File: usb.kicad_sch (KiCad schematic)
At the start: 18 parts, among them J13 USB-C_TYPE-C_16PLT-H6.5, J7 USB-A_USB-303WSD-BRY, U1 AP22615AWU-7

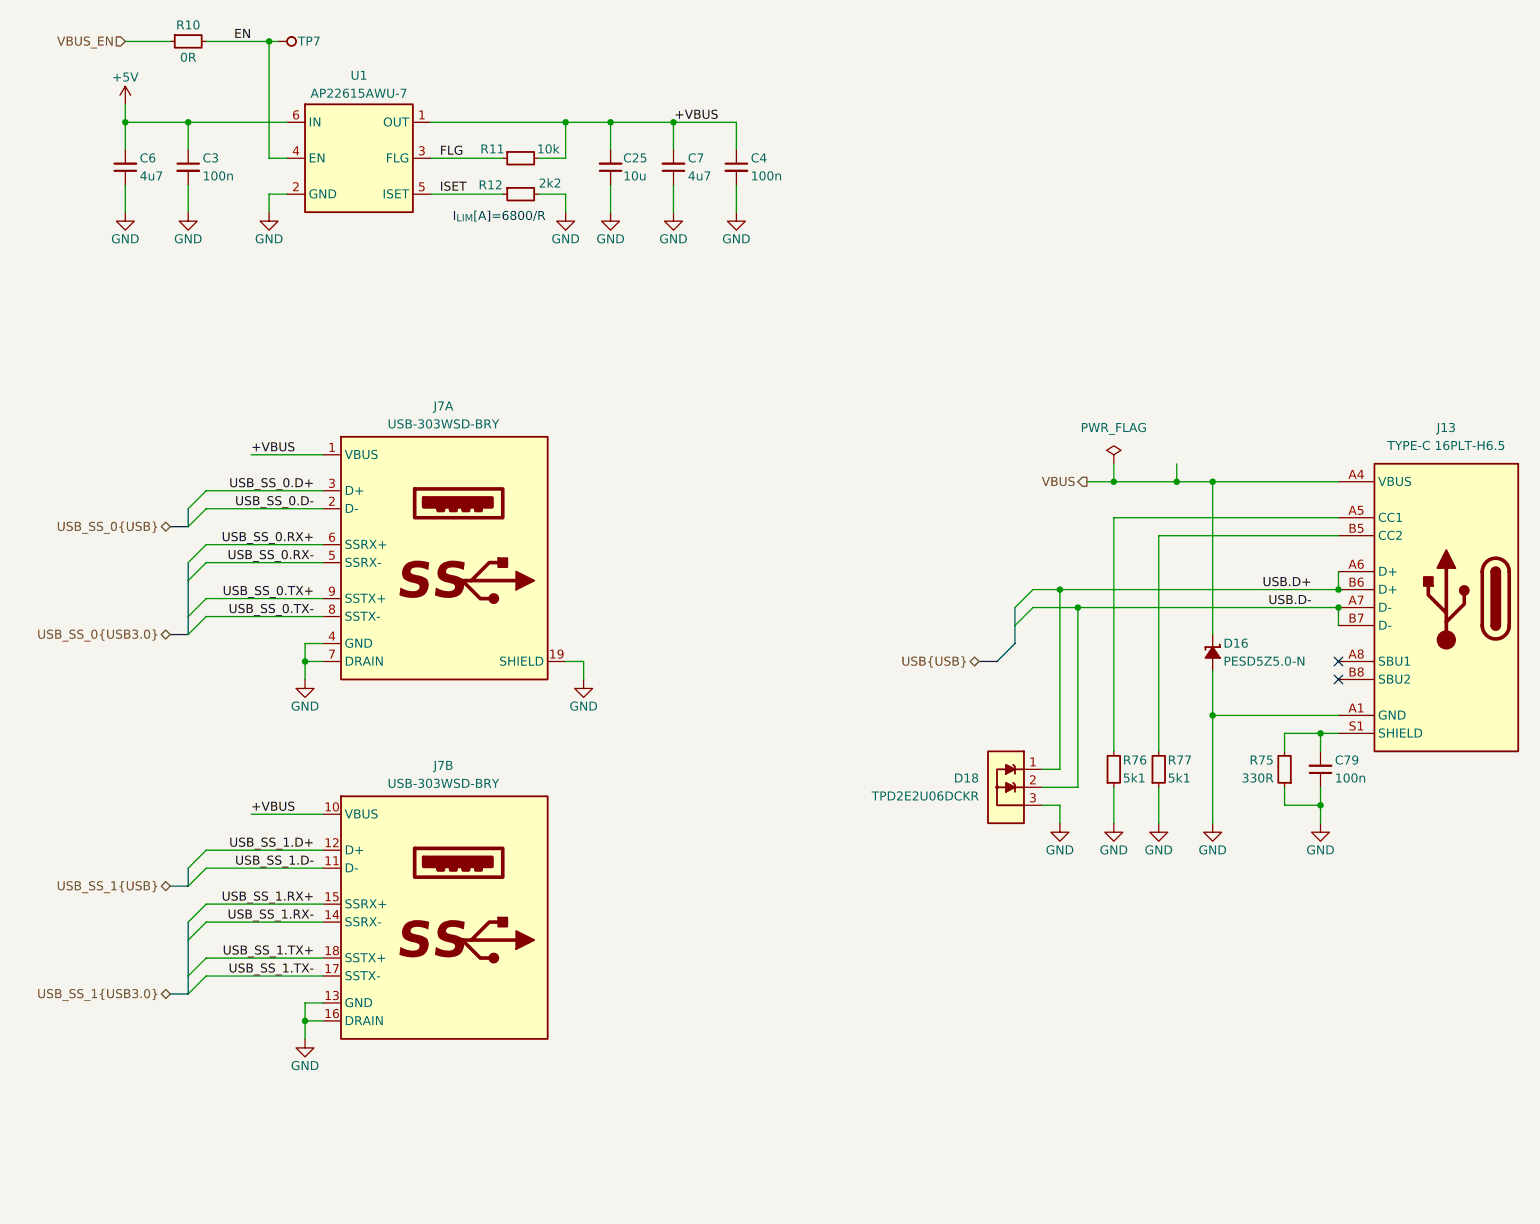
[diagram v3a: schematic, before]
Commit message: [#3] Layout HDMI, PCIe and ETH differential pairs
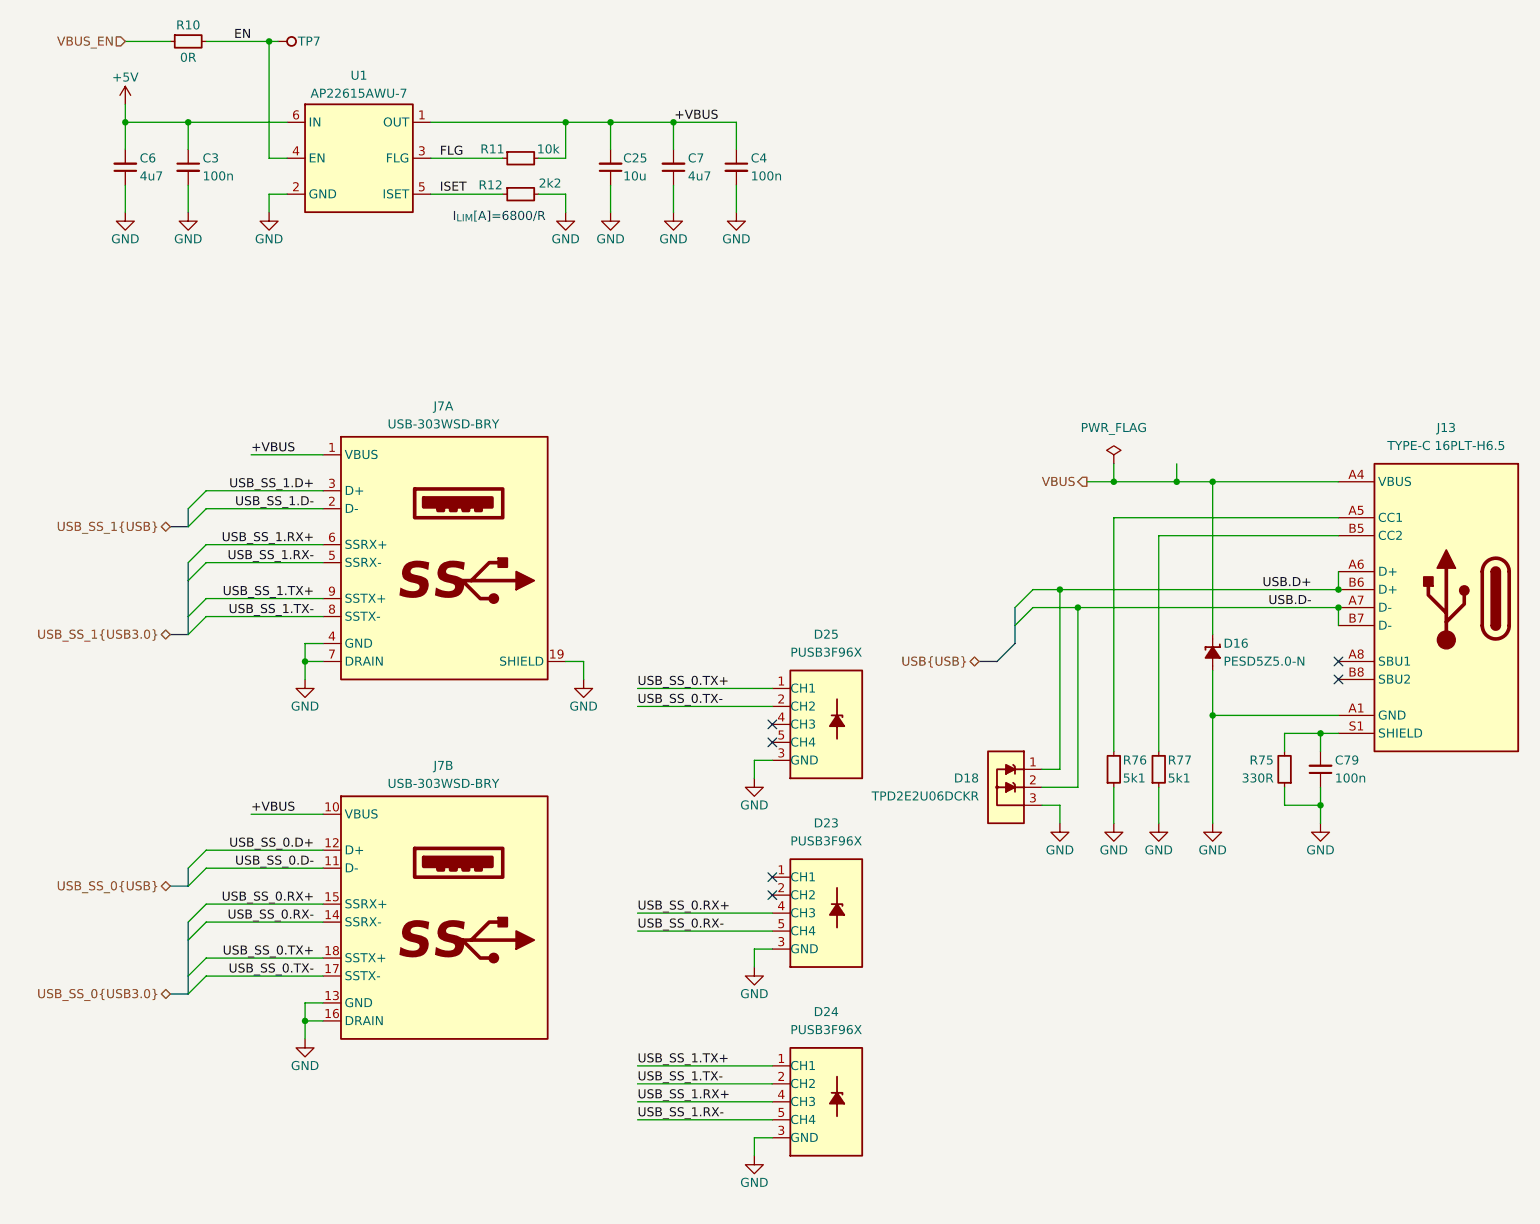
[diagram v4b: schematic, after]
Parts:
- added D23, D24, D25: PUSB3F96X, DW-footprints:SOT1176-1, symbol DW-TVS:PUSB3F96X
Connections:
- net GND: now also D23.3 (GND), D23.8 (GND), D24.3 (GND), D24.8 (GND), D25.3 (GND), D25.8 (GND)
- net USB_SS_0.D+: now also J7.12 (D+); no longer J7.3 (D+)
- net USB_SS_0.D-: now also J7.11 (D-); no longer J7.2 (D-)
- net USB_SS_0.RX+: now also J7.15 (SSRX+), D23.4 (CH3), D23.7 (CH3); no longer J7.6 (SSRX+)
- net USB_SS_0.RX-: now also J7.14 (SSRX-), D23.5 (CH4), D23.6 (CH4); no longer J7.5 (SSRX-)
- net USB_SS_0.TX+: now also J7.18 (SSTX+), D25.1 (CH1), D25.10 (CH1); no longer J7.9 (SSTX+)
- net USB_SS_0.TX-: now also J7.17 (SSTX-), D25.2 (CH2), D25.9 (CH2); no longer J7.8 (SSTX-)
- net USB_SS_1.D+: now also J7.3 (D+); no longer J7.12 (D+)
- net USB_SS_1.D-: now also J7.2 (D-); no longer J7.11 (D-)
- net USB_SS_1.RX+: now also J7.6 (SSRX+), D24.4 (CH3), D24.7 (CH3); no longer J7.15 (SSRX+)
- net USB_SS_1.RX-: now also J7.5 (SSRX-), D24.5 (CH4), D24.6 (CH4); no longer J7.14 (SSRX-)
- net USB_SS_1.TX+: now also J7.9 (SSTX+), D24.1 (CH1), D24.10 (CH1); no longer J7.18 (SSTX+)
- net USB_SS_1.TX-: now also J7.8 (SSTX-), D24.2 (CH2), D24.9 (CH2); no longer J7.17 (SSTX-)
- new net: D25.4 (CH3), D25.7 (CH3)
- new net: D25.5 (CH4), D25.6 (CH4)
- new net: D23.1 (CH1), D23.10 (CH1)
- new net: D23.2 (CH2), D23.9 (CH2)
- no-connect marks 2 -> 6

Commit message: [#3] Layout USB power
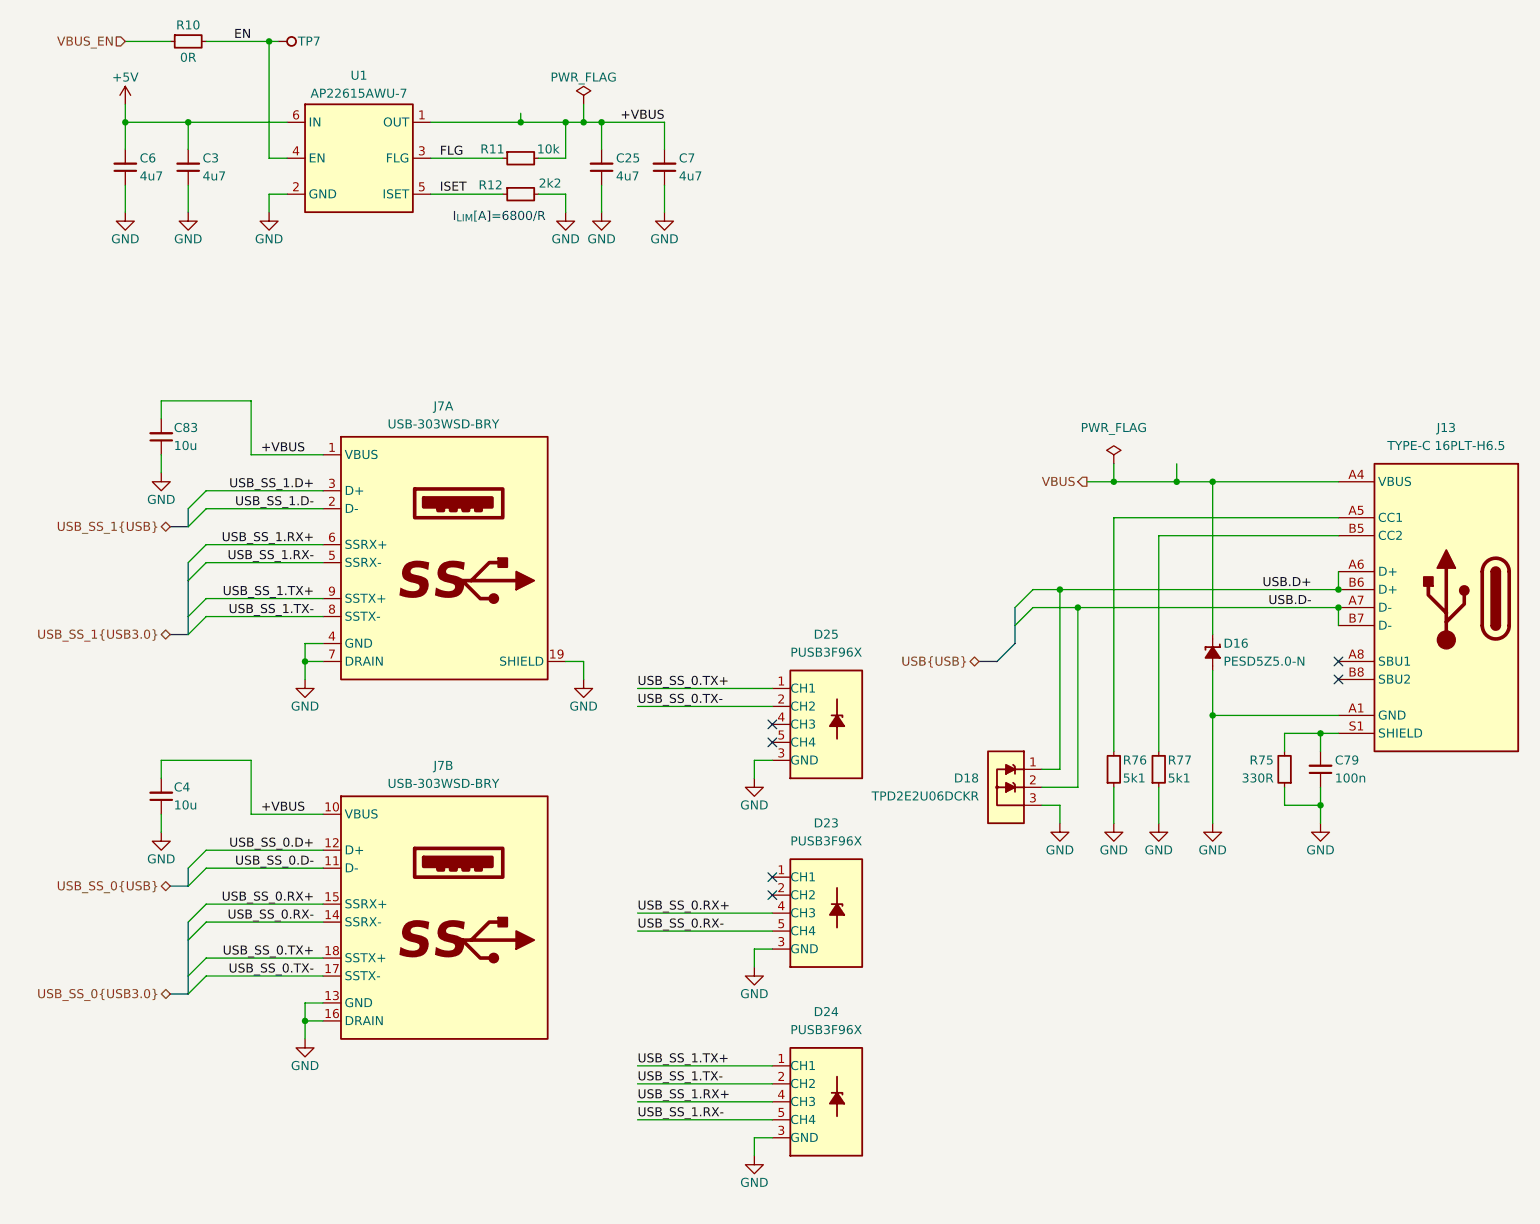
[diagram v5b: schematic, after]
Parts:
- removed C25: C-10u-0603, DW-footprints:C_0603_1608Metric, symbol DW-capacitors:C-10u-0603
- removed C3, C4: C-100n-0402, DW-footprints:C_0402_1005Metric, symbol DW-capacitors:C-100n-0402
- added C25, C3: C-4u7-0402, DW-footprints:C_0402_1005Metric, symbol DW-capacitors:C-4u7-0402
- added C4, C83: C-10u-0603, DW-footprints:C_0603_1608Metric, symbol DW-capacitors:C-10u-0603
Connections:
- net +5V: now also C3.2
- net +VBUS: now also C25.2, C4.2, C83.2
- net GND: now also C25.1, C3.1, C4.1, C83.1
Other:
- moved on the sheet: C7

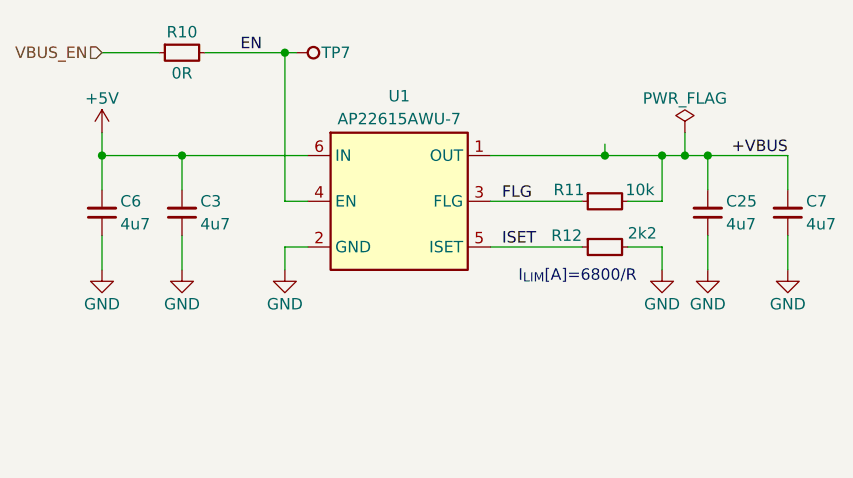
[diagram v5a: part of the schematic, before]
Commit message: [#3] Continue layout, minor schematic fixes, add power switch for CAN transceiver 5V rail
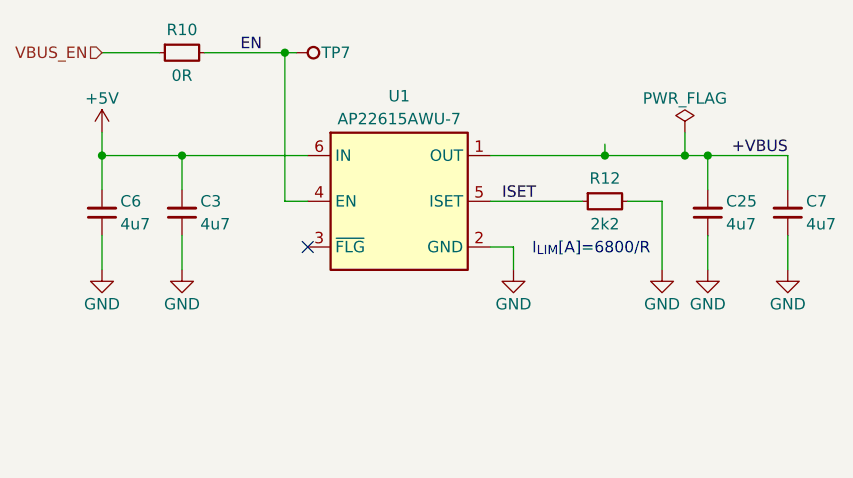
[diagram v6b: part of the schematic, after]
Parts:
- removed R11: R-10k-0402, DW-footprints:R_0402_1005Metric, symbol DW-resistors:R-10k-0402
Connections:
- net FLG: no longer names the net of U1.3 (~{FLG})
- no-connect marks 6 -> 7
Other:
- moved on the sheet: R12
